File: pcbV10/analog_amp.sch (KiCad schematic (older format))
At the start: 9 parts, among them IC1 MD8002A, J10 SPK

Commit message: pcb V10 as ordered at JLCPCB
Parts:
- added R42: 2k2, Capacitor_SMD:C_0603_1608Metric, symbol Device:R
- IC1: footprint Package_SO:SO-8_3.9x4.9mm_P1.27mm -> Package_SO:SOIC-8_3.9x4.9mm_P1.27mm
- J10: footprint Connector_PinHeader_2.54mm:PinHeader_1x02_P2.54mm_Vertical -> Connector_Wire:SolderWire-0.1sqmm_1x02_P3.6mm_D0.4mm_OD1mm
- RV1: value 5k -> 1k
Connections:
- net AUDIO: now also R42.1; no longer RV1.1
- new net: R42.2, RV1.1
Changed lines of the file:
@@
 $Descr A4 11693 8268
 encoding utf-8
-Sheet 2 3
+Sheet 2 4
 Title ""
 Date ""
@@
 F 0 "J13" H 5380 3592 50  0000 L CNN
 F 1 "SPK" H 5380 3501 50  0000 L CNN
-F 2 "Connector_PinHeader_2.54mm:PinHeader_1x02_P2.54mm_Vertical" H 5300 3600 50  0001 C CNN
+F 2 "Connector_Wire:SolderWire-0.1sqmm_1x02_P3.6mm_D0.4mm_OD1mm" H 5300 3600 50  0000 C CNN
 F 3 "~" H 5300 3600 50  0001 C CNN
 	1    5300 3600
 	1    0    0    1
 $EndComp
-Text GLabel 2900 4250 1    50   Input ~ 0
+Text GLabel 2900 3950 1    50   Input ~ 0
 AUDIO
 $Comp
@@
 P 2900 4400
 F 0 "RV1" H 2831 4446 50  0000 R CNN
-F 1 "5k" H 2831 4355 50  0000 R CNN
+F 1 "1k" H 2831 4355 50  0000 R CNN
 F 2 "Potentiometer_THT:Potentiometer_Alps_RK09K_Single_Vertical" H 2900 4400 50  0001 C CNN
 F 3 "~" H 2900 4400 50  0001 C CNN
@@
 F 0 "U18" H 4200 3765 50  0000 C CNN
 F 1 "MD8002A" H 4200 3674 50  0000 C CNN
-F 2 "Package_SO:SO-8_3.9x4.9mm_P1.27mm" H 4550 3600 50  0001 L CNN
+F 2 "Package_SO:SOIC-8_3.9x4.9mm_P1.27mm" H 4550 3600 50  0001 L CNN
 F 3 "https://www.sunrom.com/get/408862" H 4550 3500 50  0001 L CNN
 F 4 "Audio Amplifier, SOP8" H 4550 3400 50  0001 L CNN "Description"
@@
 Wire Wire Line
 	5600 3700 4700 3700
+$Comp
+L Device:R R42
+U 1 1 619968EA
+P 2900 4100
+F 0 "R42" H 2970 4146 50  0000 L CNN
+F 1 "2k2" H 2970 4055 50  0000 L CNN
+F 2 "Capacitor_SMD:C_0603_1608Metric" V 2830 4100 50  0001 C CNN
+F 3 "~" H 2900 4100 50  0001 C CNN
+F 4 "Sound only" H 2900 4100 50  0001 C CNN "Option"
+	1    2900 4100
+	1    0    0    -1
+$EndComp
 $EndSCHEMATC

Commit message: labathome v11 as ordered @ JLCPCB
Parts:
- C26: Option Sound only -> (none)
- R30: renamed from R42; footprint Capacitor_SMD:C_0603_1608Metric -> Resistor_SMD:R_0603_1608Metric
- R38, R39: footprint Capacitor_SMD:C_0603_1608Metric -> Resistor_SMD:R_0603_1608Metric
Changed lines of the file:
@@
 $Descr A4 11693 8268
 encoding utf-8
-Sheet 2 4
+Sheet 2 5
 Title ""
 Date ""
@@
 F 0 "R38" H 3570 3996 50  0000 L CNN
 F 1 "10k" H 3570 3905 50  0000 L CNN
-F 2 "Capacitor_SMD:C_0603_1608Metric" V 3430 3950 50  0001 C CNN
+F 2 "Resistor_SMD:R_0603_1608Metric" V 3430 3950 50  0001 C CNN
 F 3 "~" H 3500 3950 50  0001 C CNN
 F 4 "Sound only" H 3500 3950 50  0001 C CNN "Option"
@@
 F 0 "R39" V 4100 4150 50  0000 C CNN
 F 1 "22k" V 4200 4150 50  0000 C CNN
-F 2 "Capacitor_SMD:C_0603_1608Metric" V 4130 4150 50  0001 C CNN
+F 2 "Resistor_SMD:R_0603_1608Metric" V 4130 4150 50  0001 C CNN
 F 3 "~" H 4200 4150 50  0001 C CNN
 F 4 "Sound only" V 4200 4150 50  0001 C CNN "Option"
@@
 F 2 "Capacitor_SMD:C_0603_1608Metric" H 6188 3400 50  0001 C CNN
 F 3 "~" H 6150 3550 50  0001 C CNN
-F 4 "Sound only" H 6150 3550 50  0001 C CNN "Option"
+F 4 "" H 6150 3550 50  0001 C CNN "Option"
 	1    6150 3550
 	1    0    0    -1
@@
 	5600 3700 4700 3700
 $Comp
-L Device:R R42
+L Device:R R30
 U 1 1 619968EA
 P 2900 4100
-F 0 "R42" H 2970 4146 50  0000 L CNN
+F 0 "R30" H 2970 4146 50  0000 L CNN
 F 1 "2k2" H 2970 4055 50  0000 L CNN
-F 2 "Capacitor_SMD:C_0603_1608Metric" V 2830 4100 50  0001 C CNN
+F 2 "Resistor_SMD:R_0603_1608Metric" V 2830 4100 50  0001 C CNN
 F 3 "~" H 2900 4100 50  0001 C CNN
 F 4 "Sound only" H 2900 4100 50  0001 C CNN "Option"

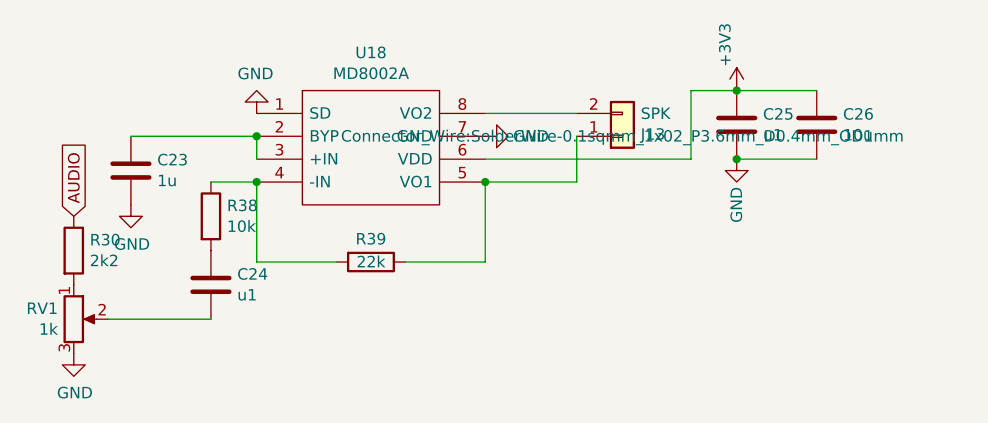
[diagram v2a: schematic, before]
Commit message: Moved all components to esp-idf components repository
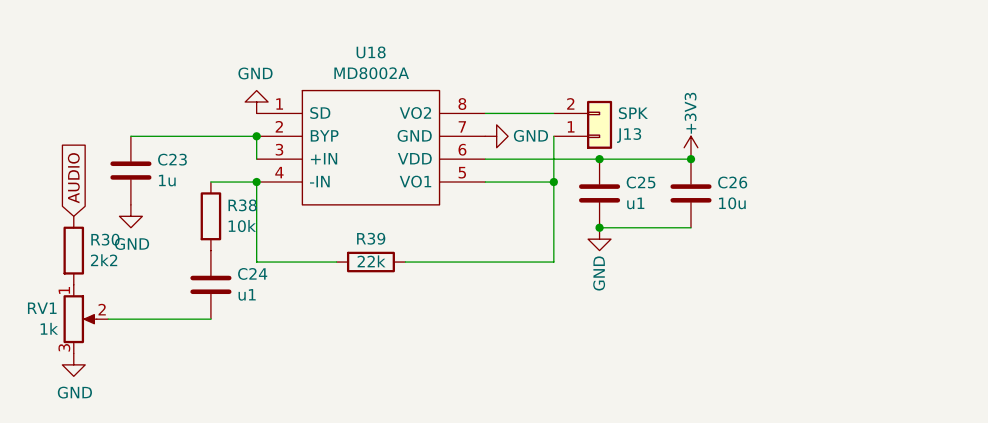
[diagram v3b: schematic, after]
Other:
- moved on the sheet: C25, C26, J13
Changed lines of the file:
@@
 L Connector_Generic:Conn_01x02 J?
 U 1 1 60B7BC42
-P 5300 3600
+P 5200 3600
 AR Path="/5FDDB245/60B7BC42" Ref="J?"  Part="1"
 AR Path="/60B762EC/60B7BC42" Ref="J10"  Part="1"
 AR Path="/61349A3C/60B7BC42" Ref="J13"  Part="1"
-F 0 "J13" H 5380 3592 50  0000 L CNN
-F 1 "SPK" H 5380 3501 50  0000 L CNN
-F 2 "Connector_Wire:SolderWire-0.1sqmm_1x02_P3.6mm_D0.4mm_OD1mm" H 5300 3600 50  0000 C CNN
-F 3 "~" H 5300 3600 50  0001 C CNN
-	1    5300 3600
+F 0 "J13" H 5280 3592 50  0000 L CNN
+F 1 "SPK" H 5280 3501 50  0000 L CNN
+F 2 "Connector_Wire:SolderWire-0.1sqmm_1x02_P3.6mm_D0.4mm_OD1mm" H 5200 3600 50  0001 C CNN
+F 3 "~" H 5200 3600 50  0001 C CNN
+	1    5200 3600
 	1    0    0    1
 $EndComp
@@
 L Device:C C25
 U 1 1 60B7E733
-P 5800 3550
-F 0 "C25" H 5915 3596 50  0000 L CNN
-F 1 "u1" H 5915 3505 50  0000 L CNN
-F 2 "Capacitor_SMD:C_0603_1608Metric" H 5838 3400 50  0001 C CNN
-F 3 "~" H 5800 3550 50  0001 C CNN
-F 4 "Sound only" H 5800 3550 50  0001 C CNN "Option"
-	1    5800 3550
+P 5200 3850
+F 0 "C25" H 5315 3896 50  0000 L CNN
+F 1 "u1" H 5315 3805 50  0000 L CNN
+F 2 "Capacitor_SMD:C_0603_1608Metric" H 5238 3700 50  0001 C CNN
+F 3 "~" H 5200 3850 50  0001 C CNN
+F 4 "Sound only" H 5200 3850 50  0001 C CNN "Option"
+	1    5200 3850
 	1    0    0    -1
 $EndComp
@@
 $EndComp
 Wire Wire Line
-	4700 3800 4700 4150
-Wire Wire Line
-	4700 4150 4350 4150
-Wire Wire Line
 	3700 3800 3700 4150
 Wire Wire Line
@@
 Connection ~ 3700 3800
 Wire Wire Line
-	4700 3500 5100 3500
-Wire Wire Line
-	4700 3800 5100 3800
-Connection ~ 4700 3800
-Wire Wire Line
-	5100 3600 5100 3800
+	4700 3500 5000 3500
+Wire Wire Line
+	4700 3800 5000 3800
+Wire Wire Line
+	5000 3600 5000 3800
 $Comp
 L power:GND #PWR0204
 U 1 1 60B9086F
-P 5800 3700
-F 0 "#PWR0204" H 5800 3450 50  0001 C CNN
-F 1 "GND" V 5800 3500 50  0000 C CNN
-F 2 "" H 5800 3700 50  0001 C CNN
-F 3 "" H 5800 3700 50  0001 C CNN
-	1    5800 3700
+P 5200 4000
+F 0 "#PWR0204" H 5200 3750 50  0001 C CNN
+F 1 "GND" V 5200 3800 50  0000 C CNN
+F 2 "" H 5200 4000 50  0001 C CNN
+F 3 "" H 5200 4000 50  0001 C CNN
+	1    5200 4000
 	1    0    0    -1
 $EndComp
@@
 L power:+3V3 #PWR0206
 U 1 1 60BA1185
-P 5800 3400
-F 0 "#PWR0206" H 5800 3250 50  0001 C CNN
-F 1 "+3V3" V 5750 3600 50  0000 C CNN
-F 2 "" H 5800 3400 50  0001 C CNN
-F 3 "" H 5800 3400 50  0001 C CNN
-	1    5800 3400
+P 5600 3700
+F 0 "#PWR0206" H 5600 3550 50  0001 C CNN
+F 1 "+3V3" V 5600 3900 50  0000 C CNN
+F 2 "" H 5600 3700 50  0001 C CNN
+F 3 "" H 5600 3700 50  0001 C CNN
+	1    5600 3700
 	1    0    0    -1
 $EndComp
@@
 L Device:C C26
 U 1 1 60B8A568
-P 6150 3550
-F 0 "C26" H 6265 3596 50  0000 L CNN
-F 1 "10u" H 6265 3505 50  0000 L CNN
-F 2 "Capacitor_SMD:C_0603_1608Metric" H 6188 3400 50  0001 C CNN
-F 3 "~" H 6150 3550 50  0001 C CNN
-F 4 "" H 6150 3550 50  0001 C CNN "Option"
-	1    6150 3550
-	1    0    0    -1
-$EndComp
-Wire Wire Line
-	6150 3400 5800 3400
-Wire Wire Line
-	6150 3700 5800 3700
-Connection ~ 5800 3700
-Connection ~ 5800 3400
-Wire Wire Line
-	5800 3400 5600 3400
-Wire Wire Line
-	5600 3400 5600 3700
-Wire Wire Line
-	5600 3700 4700 3700
+P 5600 3850
+F 0 "C26" H 5715 3896 50  0000 L CNN
+F 1 "10u" H 5715 3805 50  0000 L CNN
+F 2 "Capacitor_SMD:C_0603_1608Metric" H 5638 3700 50  0001 C CNN
+F 3 "~" H 5600 3850 50  0001 C CNN
+F 4 "" H 5600 3850 50  0001 C CNN "Option"
+	1    5600 3850
+	1    0    0    -1
+$EndComp
+Wire Wire Line
+	5600 3700 5200 3700
+Wire Wire Line
+	5600 4000 5200 4000
+Connection ~ 5200 4000
+Connection ~ 5200 3700
 $Comp
 L Device:R R30
@@
 	1    0    0    -1
 $EndComp
+Wire Wire Line
+	4700 3700 5200 3700
+Connection ~ 5600 3700
+Wire Wire Line
+	5000 3800 5000 4150
+Connection ~ 5000 3800
+Wire Wire Line
+	4350 4150 5000 4150
 $EndSCHEMATC
